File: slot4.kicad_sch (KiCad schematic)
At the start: 1 part

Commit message: board layout
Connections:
- net AD1: now also PL4.a3 (Pin_a3); no longer PL4.b3 (Pin_b3)
- net Chroma: now also PL4.a2 (Pin_a2); no longer PL4.b2 (Pin_b2)
- net GND: now also PL4.b3 (Pin_b3); no longer PL4.a3 (Pin_a3)
- net Luma: now also PL4.b2 (Pin_b2); no longer PL4.a2 (Pin_a2)
- net VCLK: now reaches PL4.a38 (Pin_a38)
- net ESND: now reaches PL4.b10 (Pin_b10)
- no-connect marks 1 -> 0

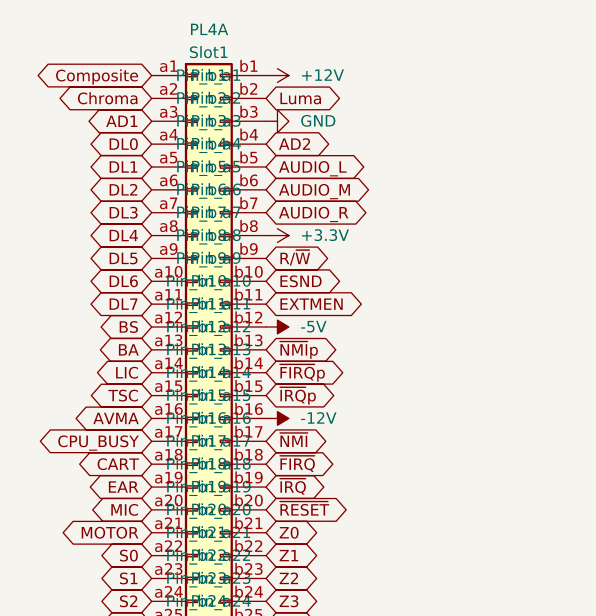
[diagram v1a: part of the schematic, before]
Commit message: revise bus tracing
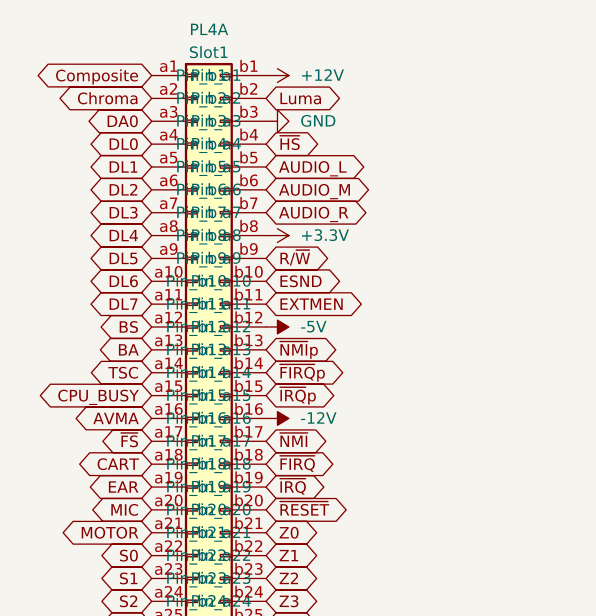
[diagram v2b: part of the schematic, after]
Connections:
- net LIC is gone; now on net TSC: PL4.a14 (Pin_a14)
- net CPU_BUSY: now also PL4.a15 (Pin_a15); no longer PL4.a17 (Pin_a17)
- net TSC: no longer PL4.a15 (Pin_a15)
- net AD1 renamed DA0
- net AD2 renamed ~{HS}
- new net ~{FS}: PL4.a17 (Pin_a17)
